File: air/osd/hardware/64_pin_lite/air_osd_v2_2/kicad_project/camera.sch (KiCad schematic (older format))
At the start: 4 parts, among them K1 SIL3

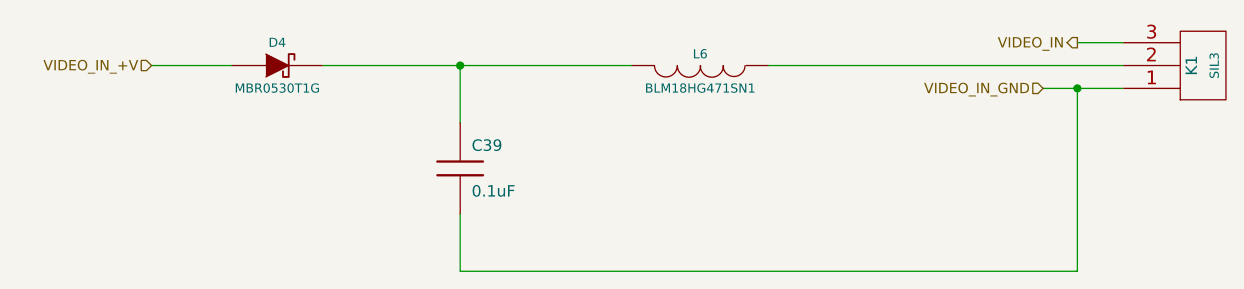
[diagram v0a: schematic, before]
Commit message: added Fiducials and settings to get pos file
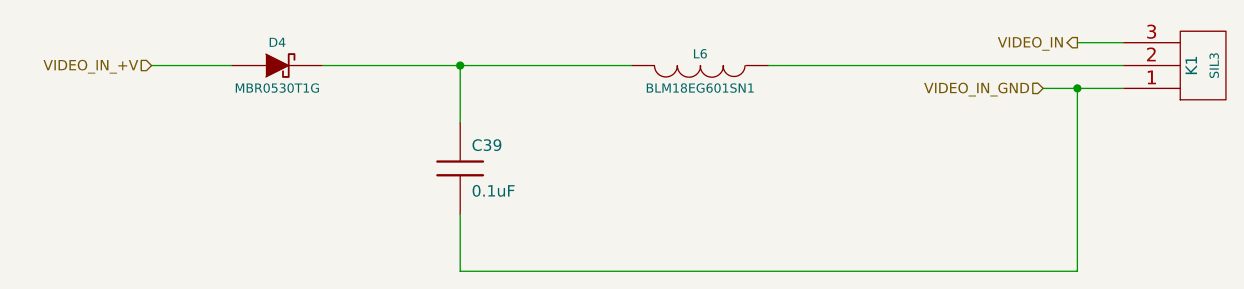
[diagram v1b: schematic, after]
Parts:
- L6: value BLM18HG471SN1 -> BLM18EG601SN1; MFG Part Num BLM18HG471SN1 -> BLM18EG601SN1
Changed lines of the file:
@@
-EESchema Schematic File Version 2  date Thu 18 Jun 2015 19:52:51 BST
+EESchema Schematic File Version 2  date Fri 19 Jun 2015 22:46:51 BST
 LIBS:lm358
 LIBS:conn_6
@@
 LIBS:R0link
 LIBS:emi_filter
+LIBS:fiducial
+LIBS:osd-cache
 EELAYER 25  0
 EELAYER END
@@
 Sheet 4 8
 Title ""
-Date "18 jun 2015"
+Date "19 jun 2015"
 Rev ""
 Comp ""
@@
 P 5100 3450
 F 0 "L6" V 5050 3450 40  0000 C CNN
-F 1 "BLM18HG471SN1" V 5200 3450 40  0000 C CNN
+F 1 "BLM18EG601SN1" V 5200 3450 40  0000 C CNN
 F 2 "0603" H 5100 3450 60  0001 C CNN
 F 3 "D" H 5100 3450 60  0001 C CNN
 F 4 "Murata" H 5100 3450 60  0001 C CNN "MFG Name"
-F 5 "BLM18HG471SN1" H 5100 3450 60  0001 C CNN "MFG Part Num"
+F 5 "BLM18EG601SN1" H 5100 3450 60  0001 C CNN "MFG Part Num"
 F 6 "EMI Suppression filter" H 5100 3450 60  0001 C CNN "Description"
 	1    5100 3450
@@
 	4050 4350 4050 4100
 Wire Wire Line
-	4800 3450 4050 3450
-Wire Wire Line
-	4050 3450 3450 3450
+	4800 3450 3450 3450
 Wire Wire Line
 	5400 3450 6950 3450
@@
 	6950 3350 6750 3350
 Wire Wire Line
-	6600 3550 6750 3550
-Wire Wire Line
-	6750 3550 6950 3550
+	6600 3550 6950 3550
 Wire Wire Line
 	3050 3450 2700 3450
